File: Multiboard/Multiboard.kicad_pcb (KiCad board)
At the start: 2 copper layers, 120 x 120 mm, 88 parts, among them J1 Conn_01x20_Socket, J2 Conn_01x20_Socket, J3 Debug, J4 USB_C_Receptacle_USB2.0_16P, Q1 Q_Dual_NMOS_G1S2G2D2S1D1, Q14 Q_Dual_NMOS_G1S2G2D2S1D1, Q3 Q_Dual_NMOS_G1S2G2D2S1D1, Q4 Q_Dual_NMOS_G1S2G2D2S1D1, Q5 Q_Dual_NMOS_G1S2G2D2S1D1, Q6 Q_Dual_NMOS_G1S2G2D2S1D1, Q7 Q_Dual_NMOS_G1S2G2D2S1D1, SW1 BOOT0, SW2 NRST, SW3 SW_SPST, SW4 SW_SPST, SW5 SW_SPST, SW7 SW_SPST, SW8 KEY, SW9 SW_SPST, U1 STM32F411RET6, U2 MAX662AESA_T, U3 MCP1792x-3302xCB, Y1 32.768KHz, Y2 25MHz

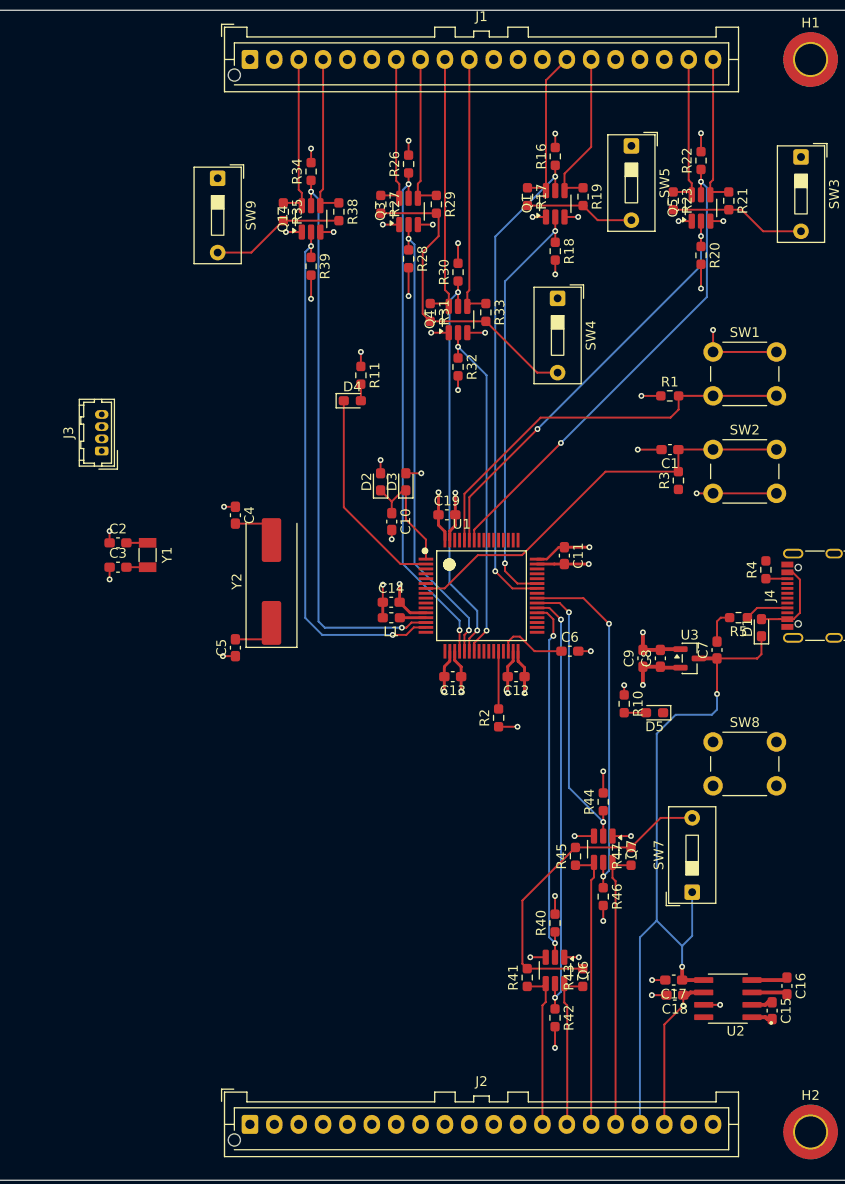
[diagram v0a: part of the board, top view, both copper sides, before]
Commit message: wired most of the gpio pins
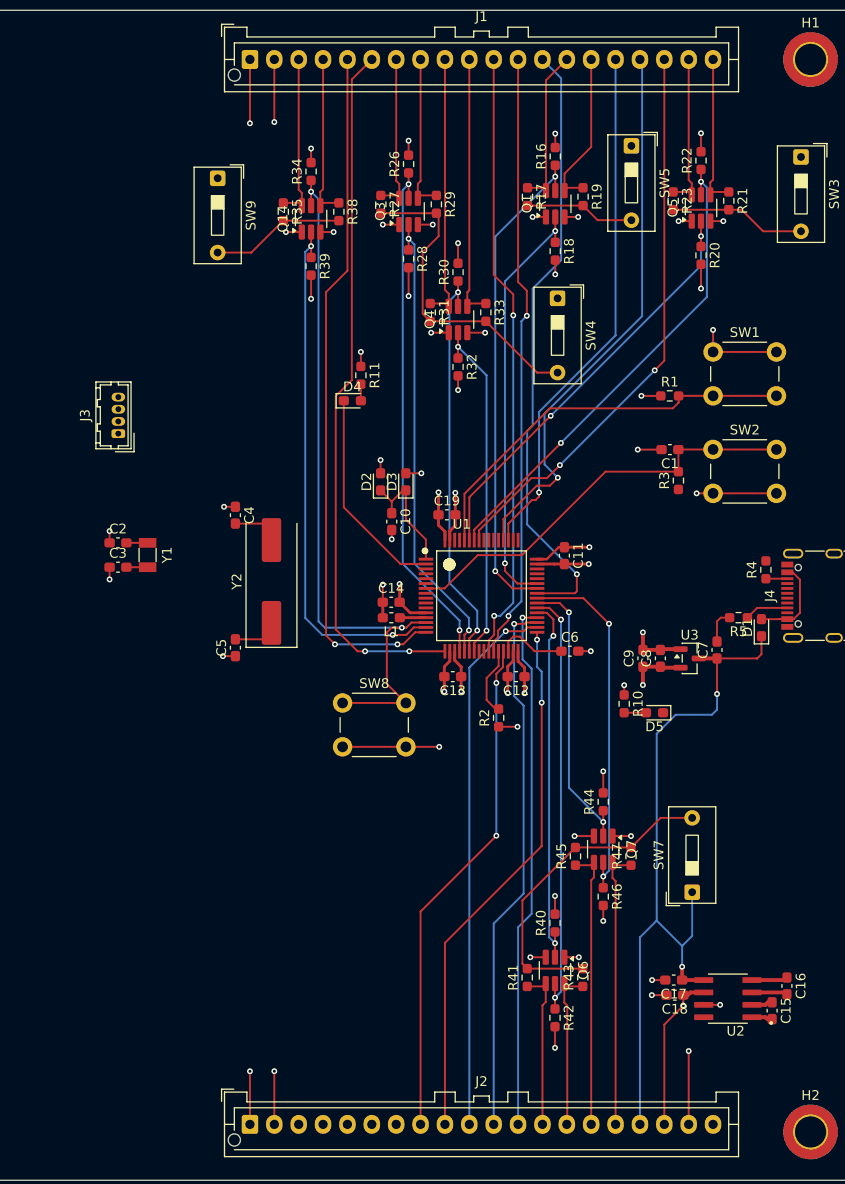
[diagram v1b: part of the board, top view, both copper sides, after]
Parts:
- moved SW8 38.2 mm to (107.0, 111.0)
- moved J3 2.46 mm to (84.0, 83.4)
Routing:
- net Net-(J1-Pin_6): track 0.00 -> 72.1 mm, vias 0 -> 2
- net Net-(J1-Pin_5): track 0.00 -> 71.1 mm, vias 0 -> 2
- net /PA8: track 0.00 -> 63.1 mm, vias 0 -> 1
- net /PB0: track 0.00 -> 62.9 mm, vias 0 -> 2
- net /PB1: track 0.00 -> 62.5 mm, vias 0 -> 2
- net /PB5: track 0.00 -> 58.1 mm, vias 0 -> 2
- net /PC11: track 0.00 -> 57.2 mm, vias 0 -> 1
- net /PB13: track 0.00 -> 55.5 mm, vias 0 -> 1
- net /PB14: track 0.00 -> 55.4 mm, vias 0 -> 1
- net /PB12: track 0.00 -> 54.8 mm, vias 0 -> 2
- net /PB15: track 0.00 -> 54.4 mm, vias 0 -> 1
- net /PC10: track 0.00 -> 54.1 mm, vias 0 -> 1
- net /PB10: track 0.00 -> 52.0 mm, vias 0 -> 2
- net GND: track 59.8 -> 89.1 mm, vias 19 -> 23
- net PA0-MCU: track 58.5 -> 74.8 mm
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
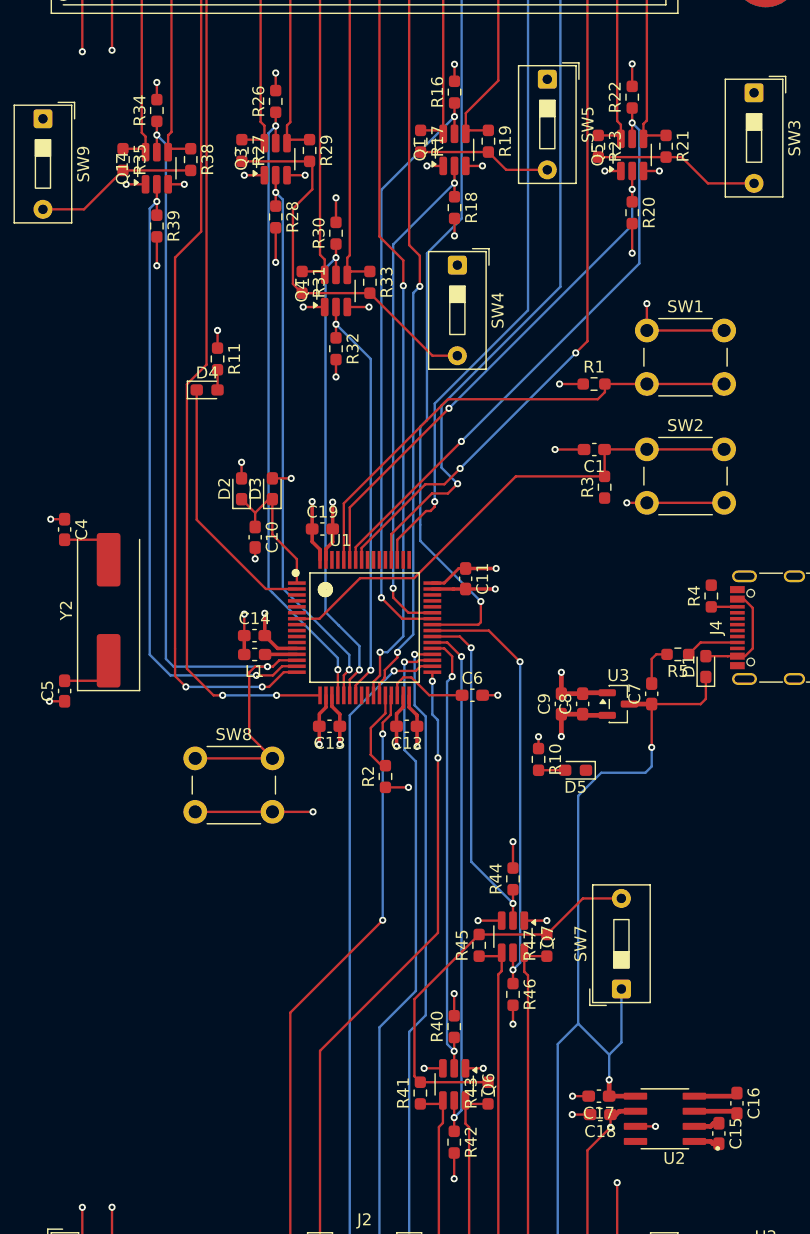
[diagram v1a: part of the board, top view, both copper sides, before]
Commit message: Wired usb
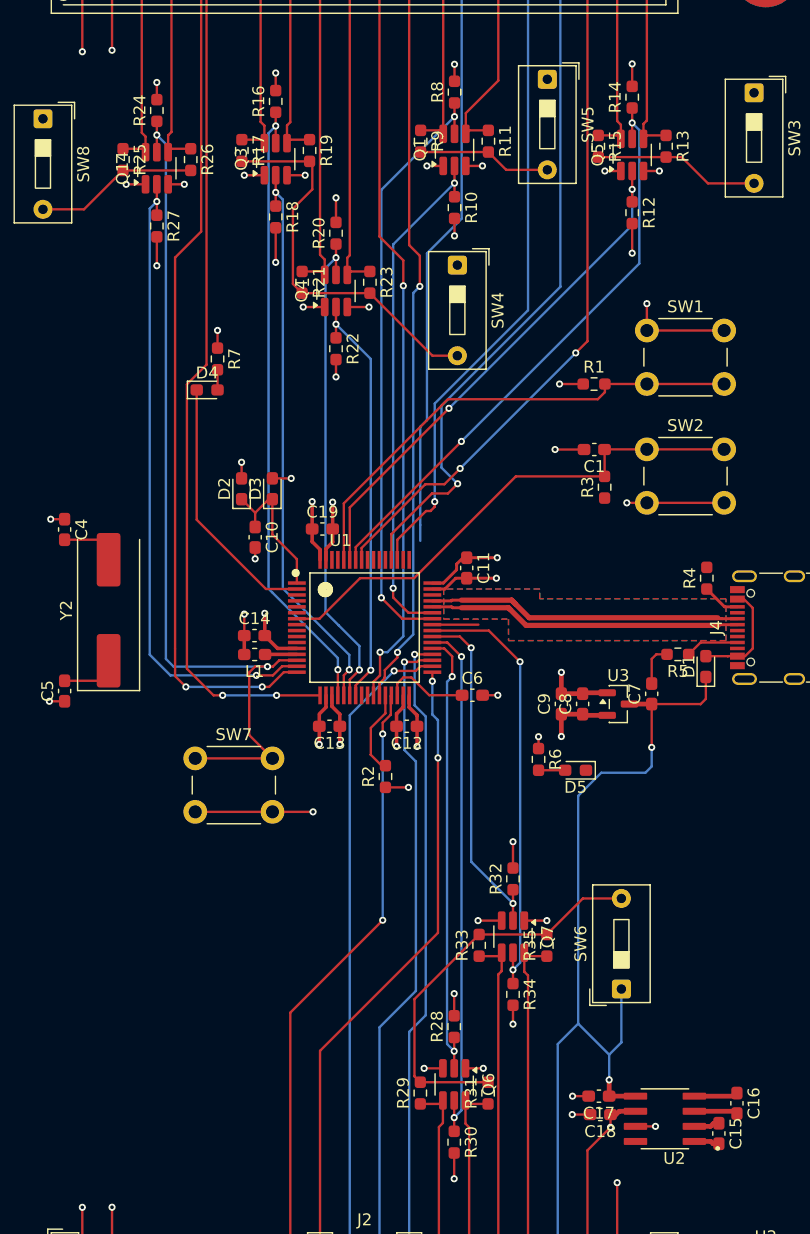
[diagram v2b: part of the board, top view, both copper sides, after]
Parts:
- moved R4 1.55 mm to (150.0, 95.8)
- moved C11 0.91 mm to (129.8, 95.0)
- renumbered R18 to R10, R19 to R11, R20 to R12, R21 to R13, R22 to R14, R23 to R15, R26 to R16, R27 to R17, R28 to R18, R29 to R19, R30 to R20, R31 to R21, R32 to R22, R33 to R23, R34 to R24, R35 to R25, R38 to R26, R39 to R27, R40 to R28, R41 to R29, R42 to R30, R43 to R31, R44 to R32, R45 to R33, R46 to R34, R47 to R35, R10 to R6, R11 to R7, R16 to R8, R17 to R9, SW7 to SW6, SW8 to SW7, SW9 to SW8
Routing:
- net /D+: track 0.00 -> 26.8 mm
- net /D-: track 0.00 -> 26.5 mm
- net /PA8: track 63.1 -> 53.8 mm, vias 1 -> 0
- net Net-(J4-CC2): track 2.20 -> 3.20 mm
- added copper zone on B.Cu, net GND
- added copper zone on F.Cu, net GND

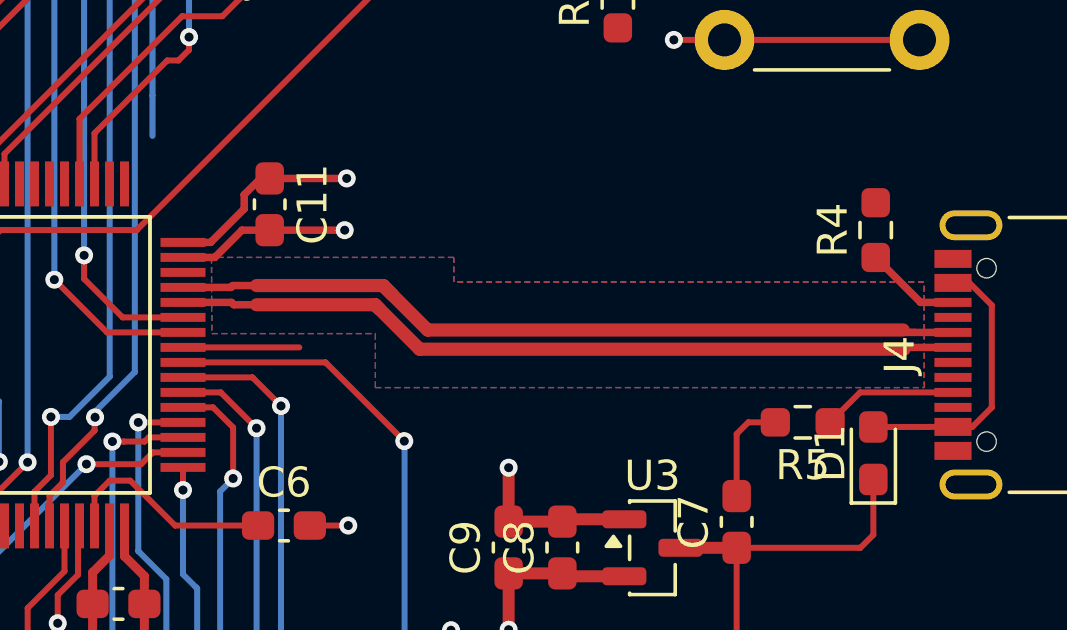
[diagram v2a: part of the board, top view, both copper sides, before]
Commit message: Implemented FTDI in schematic
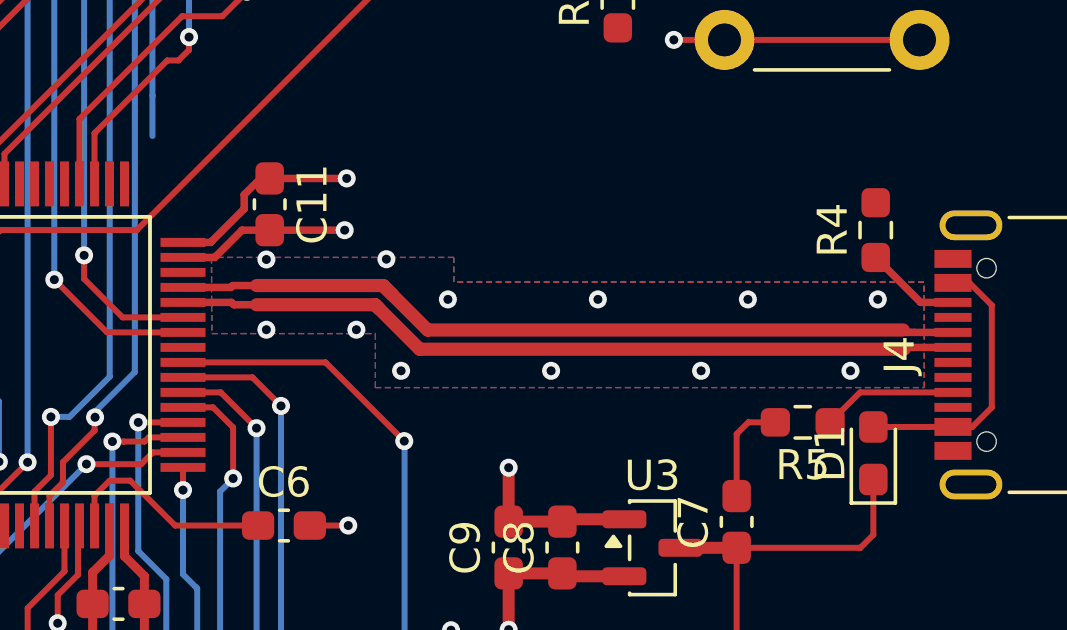
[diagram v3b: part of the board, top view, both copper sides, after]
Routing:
- net /PA8: track 53.8 -> 49.9 mm
- net GND: vias 23 -> 35
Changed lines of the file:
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@@
+	)
+	(via
+		(at 129.73 96.82)
+		(size 0.6)
+		(drill 0.3)
+		(layers "F.Cu" "B.Cu")
+		(free yes)
+		(net 1)
 	)
 	(via
@@
 	)
 	(via
+		(at 149.2 100.53)
+		(size 0.6)
+		(drill 0.3)
+		(layers "F.Cu" "B.Cu")
+		(free yes)
+		(net 1)
+	)
+	(via
 		(at 112.043 94.212)
 		(size 0.6)
@@
 	)
 	(via
+		(at 144.22 100.53)
+		(size 0.6)
+		(drill 0.3)
+		(layers "F.Cu" "B.Cu")
+		(free yes)
+		(net 1)
+	)
+	(via
+		(at 129.73 99.16)
+		(size 0.6)
+		(drill 0.3)
+		(layers "F.Cu" "B.Cu")
+		(free yes)
+		(net 1)
+	)
+	(via
 		(at 143.312 89.5)
 		(size 0.6)
@@
 	)
 	(via
+		(at 133.73 96.81)
+		(size 0.6)
+		(drill 0.3)
+		(layers "F.Cu" "B.Cu")
+		(free yes)
+		(net 1)
+	)
+	(via
 		(at 123.9375 109.9915)
 		(size 0.6)
@@
 	)
 	(via
+		(at 139.22 100.53)
+		(size 0.6)
+		(drill 0.3)
+		(layers "F.Cu" "B.Cu")
+		(free yes)
+		(net 1)
+	)
+	(via
+		(at 150.11 98.15)
+		(size 0.6)
+		(drill 0.3)
+		(layers "F.Cu" "B.Cu")
+		(free yes)
+		(net 1)
+	)
+	(via
 		(at 112.8515 98.7965)
 		(size 0.6)
@@
 	)
 	(via
+		(at 134.22 100.53)
+		(size 0.6)
+		(drill 0.3)
+		(layers "F.Cu" "B.Cu")
+		(free yes)
+		(net 1)
+	)
+	(via
 		(at 132.459 105.688)
 		(size 0.6)
@@
 	)
 	(via
+		(at 145.78 98.15)
+		(size 0.6)
+		(drill 0.3)
+		(layers "F.Cu" "B.Cu")
+		(free yes)
+		(net 1)
+	)
+	(via
 		(at 137.65 79.504)
 		(size 0.6)
@@
 	)
 	(via
+		(at 132.73 99.16)
+		(size 0.6)
+		(drill 0.3)
+		(layers "F.Cu" "B.Cu")
+		(free yes)
+		(net 1)
+	)
+	(via
 		(at 100 148.767)
 		(size 0.6)
@@
 	)
 	(via
+		(at 140.78 98.15)
+		(size 0.6)
+		(drill 0.3)
+		(layers "F.Cu" "B.Cu")
+		(free yes)
+		(net 1)
+	)
+	(via
 		(at 118.5625 89.4425)
 		(size 0.6)
@@
 		(drill 0.3)
 		(layers "F.Cu" "B.Cu")
+		(net 1)
+	)
+	(via
+		(at 135.78 98.15)
+		(size 0.6)
+		(drill 0.3)
+		(layers "F.Cu" "B.Cu")
+		(free yes)
 		(net 1)
 	)
@@
 	)
 	(segment
-		(start 130.829 99.75)
-		(end 126.95 99.75)
-		(width 0.2)
-		(layer "F.Cu")
-		(net 32)
-	)
-	(segment

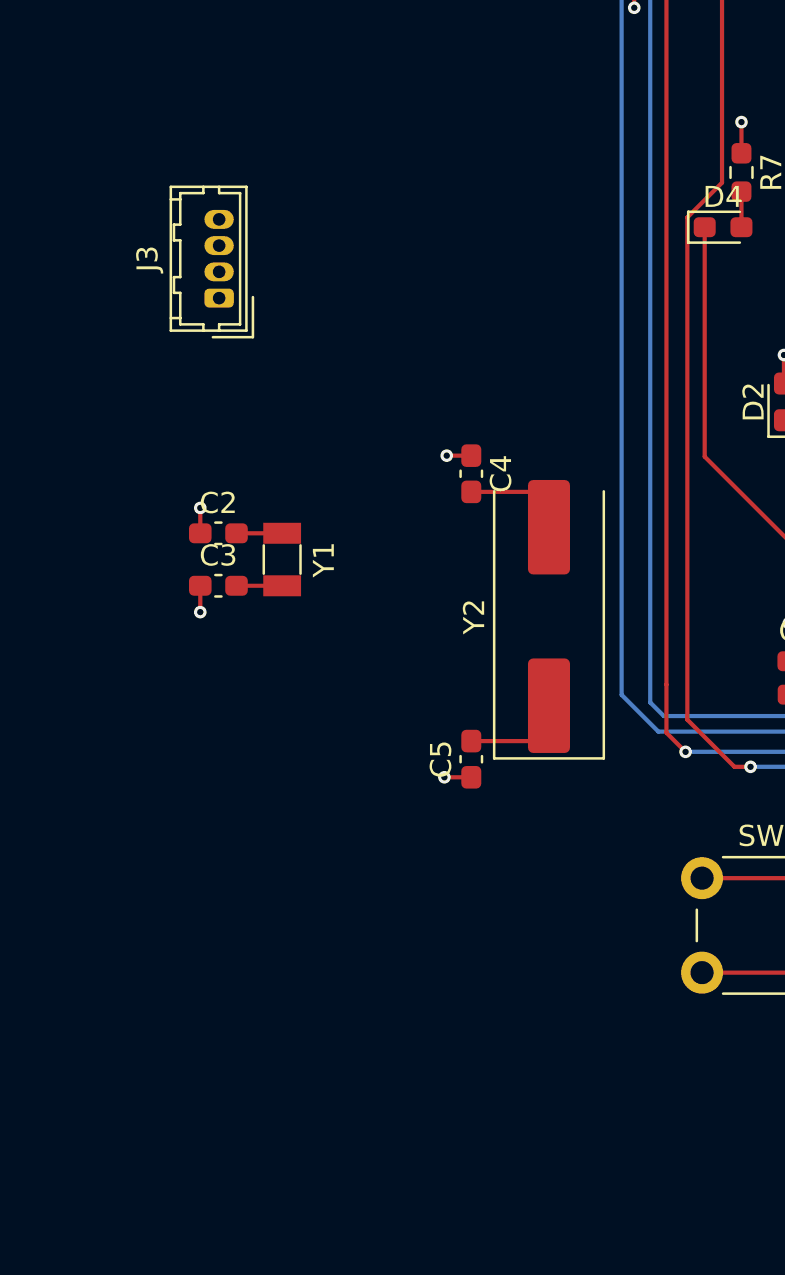
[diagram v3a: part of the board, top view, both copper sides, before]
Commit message: Added footprints and fixed schematic
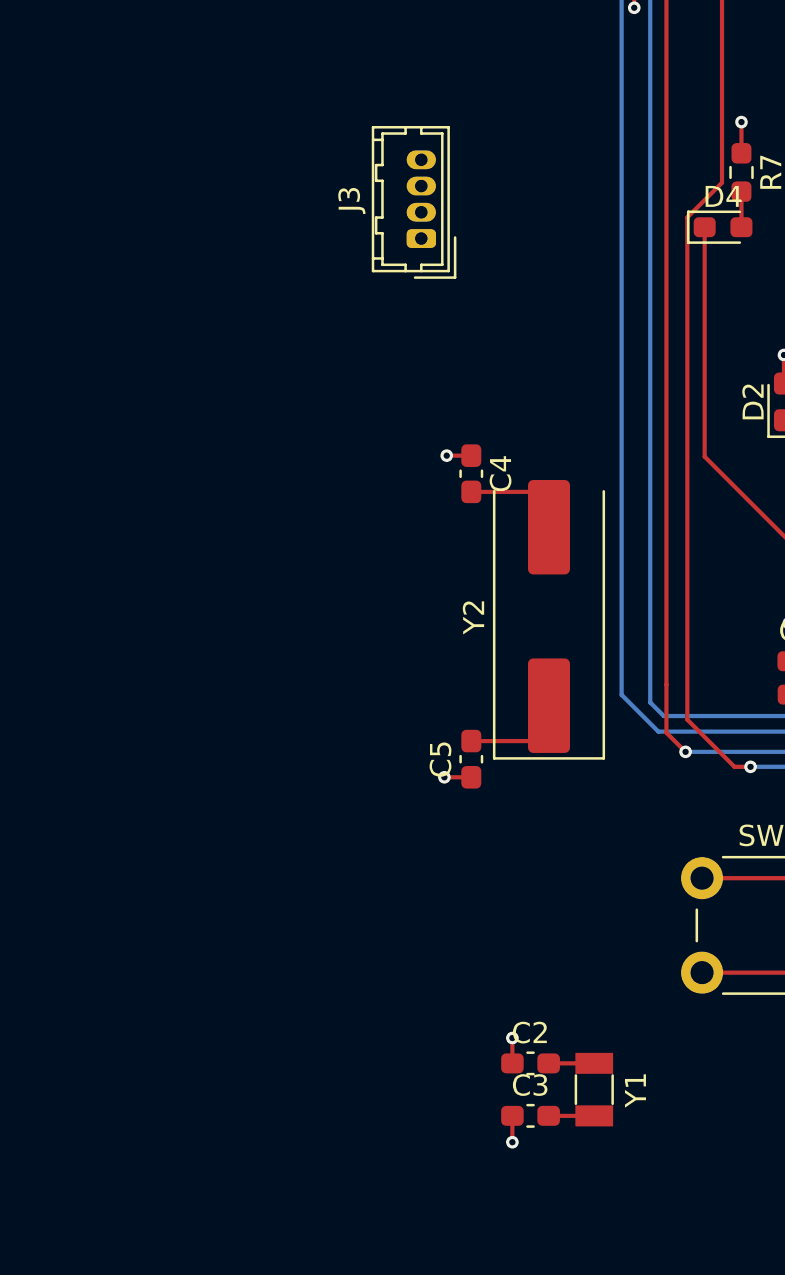
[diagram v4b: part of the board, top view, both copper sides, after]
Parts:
- moved C2 29.3 mm to (98.8, 119.8)
- moved C3 29.3 mm to (98.8, 122.3)
- moved Y1 29.3 mm to (101.9, 121.1)
- moved J3 10.0 mm to (93.6, 80.5)
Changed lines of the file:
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@@
 	(footprint "Crystal:Crystal_SMD_3215-2Pin_3.2x1.5mm"
 		(layer "F.Cu")
-		(at 87.0025 95.826 -90)
+		(at 101.86625 121.07 -90)
 		(descr "SMD Crystal FC-135 https://support.epson.biz/td/api/doc_check.php?dl=brief_FC-135R_en.pdf")
 		(tags "SMD SMT Crystal")
@@
 	(footprint "Capacitor_SMD:C_0603_1608Metric_Pad1.08x0.95mm_HandSolder"
 		(layer "F.Cu")
-		(at 83.9665 97.075)
+		(at 98.83025 122.319)
 		(descr "Capacitor SMD 0603 (1608 Metric), square (rectangular) end terminal, IPC-7351 nominal with elongated pad for handsoldering. (Body size source: IPC-SM-782 page 76, https://www.pcb-3d.com/wordpress/wp-content/uploads/ipc-sm-782a_amendment_1_and_2.pdf), generated with kicad-footprint-generator")
 		(tags "capacitor handsolder")
@@
 	(footprint "Connector_Hirose:Hirose_DF13-04P-1.25DSA_1x04_P1.25mm_Vertical"
 		(layer "F.Cu")
-		(at 84.001 83.377 90)
+		(at 93.63 80.54 90)
 		(descr "Hirose DF13 through hole, DF13-04P-1.25DSA, 4 Pins per row (https://www.hirose.com/product/en/products/DF13/DF13-2P-1.25DSA%2850%29/), generated with kicad-footprint-generator")
 		(tags "connector Hirose DF13 vertical")
@@
 	(footprint "Capacitor_SMD:C_0603_1608Metric_Pad1.08x0.95mm_HandSolder"
 		(layer "F.Cu")
-		(at 83.9665 94.577)
+		(at 98.83025 119.821)
 		(descr "Capacitor SMD 0603 (1608 Metric), square (rectangular) end terminal, IPC-7351 nominal with elongated pad for handsoldering. (Body size source: IPC-SM-782 page 76, https://www.pcb-3d.com/wordpress/wp-content/uploads/ipc-sm-782a_amendment_1_and_2.pdf), generated with kicad-footprint-generator")
 		(tags "capacitor handsolder")
@@
 	)
 	(segment
-		(start 83.104 94.577)
-		(end 83.104 93.3695)
+		(start 97.96775 119.821)
+		(end 97.96775 118.6135)
 		(width 0.2)
 		(layer "F.Cu")
@@
 	)
 	(segment
-		(start 83.104 97.075)
-		(end 83.104 98.3305)
+		(start 97.96775 122.319)
+		(end 97.96775 123.5745)
 		(width 0.2)
 		(layer "F.Cu")
@@
 	)
 	(via
-		(at 83.104 93.3695)
+		(at 97.96775 118.6135)
 		(size 0.6)
 		(drill 0.3)
@@
 	)
 	(via
-		(at 83.104 98.3305)
+		(at 97.96775 123.5745)
 		(size 0.6)
 		(drill 0.3)
@@
 	)
 	(segment
-		(start 87.0025 94.576)
-		(end 84.83 94.576)
+		(start 101.86625 119.82)
+		(end 99.69375 119.82)
 		(width 0.2)
 		(layer "F.Cu")
@@
 	)
 	(segment
-		(start 84.83 94.576)
-		(end 84.829 94.577)
+		(start 99.69375 119.82)
+		(end 99.69275 119.821)
 		(width 0.2)
 		(layer "F.Cu")
@@
 	)
 	(segment
-		(start 87.0025 97.076)
-		(end 84.83 97.076)
+		(start 101.86625 122.32)
+		(end 99.69375 122.32)
 		(width 0.2)
 		(layer "F.Cu")
@@
 	)
 	(segment
-		(start 84.83 97.076)
-		(end 84.829 97.075)
+		(start 99.69375 122.32)
+		(end 99.69275 122.319)
 		(width 0.2)
 		(layer "F.Cu")
